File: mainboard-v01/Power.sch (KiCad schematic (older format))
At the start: 37 parts, among them Q15 IRLML2803, U11 NDS8434, U5 MAX4372TEUK+T, U6 LTC4121-4.2, U7 TPS54226PWPRPWP14_2P31X2P46-L

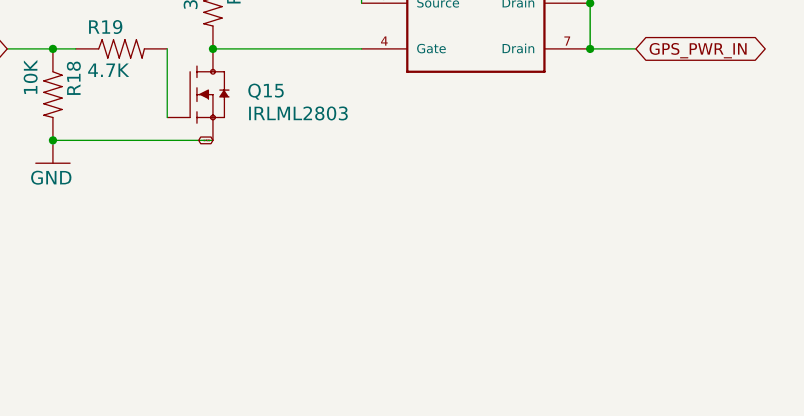
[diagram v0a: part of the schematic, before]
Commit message: adding v01 schematic pdf
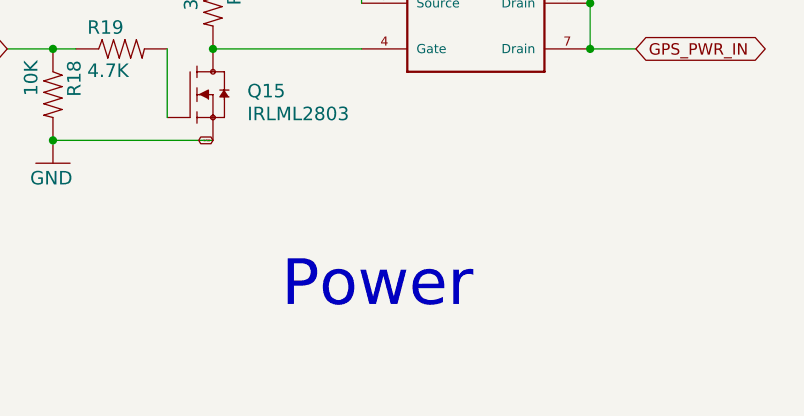
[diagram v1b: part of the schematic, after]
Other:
- note added: "Power"
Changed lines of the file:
@@
 Wire Wire Line
 	10300 5600 10300 5800
+Text Notes 8950 6950 0    200  ~ 0
+Power
 $EndSCHEMATC
